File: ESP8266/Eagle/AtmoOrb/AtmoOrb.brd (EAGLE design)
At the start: 55.9 x 55.9 mm, 10 parts, among them J1 DCJ0202

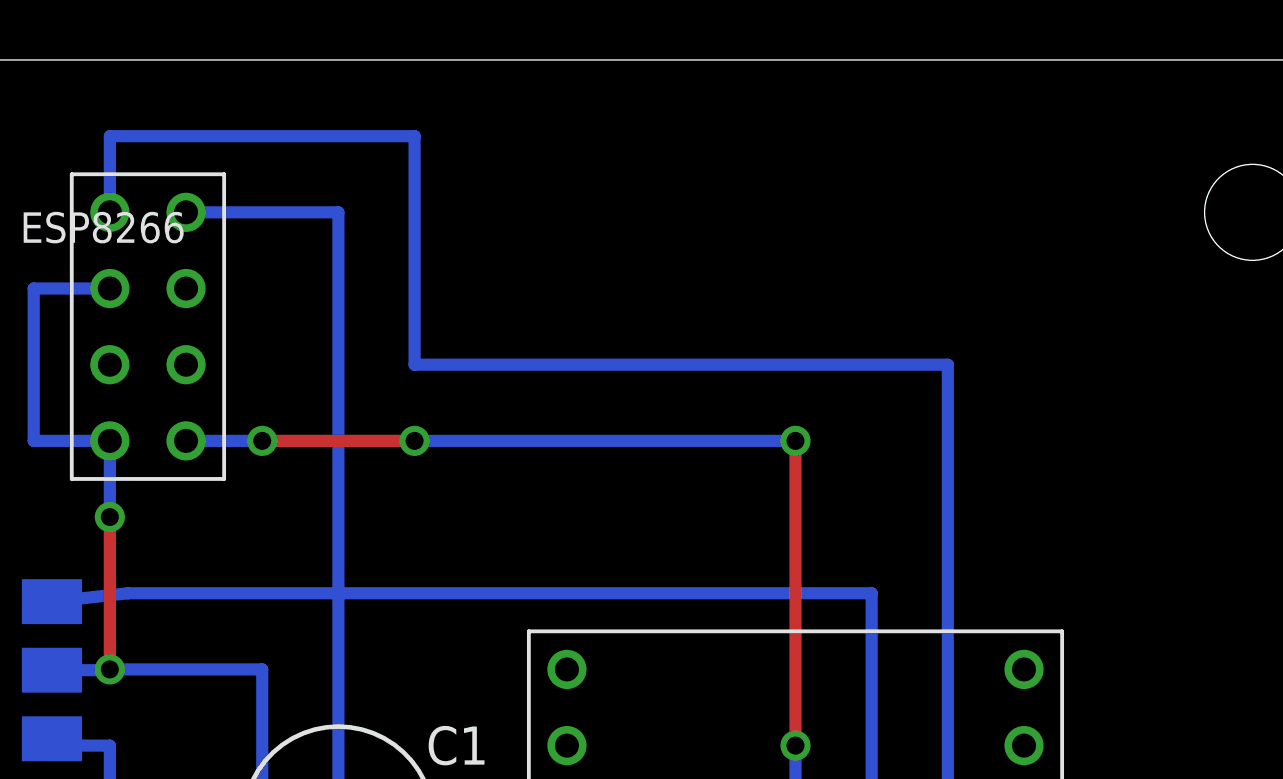
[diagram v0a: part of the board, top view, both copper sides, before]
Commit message: Added a switch to bring ESP8266 into update mode to schematic and board layout
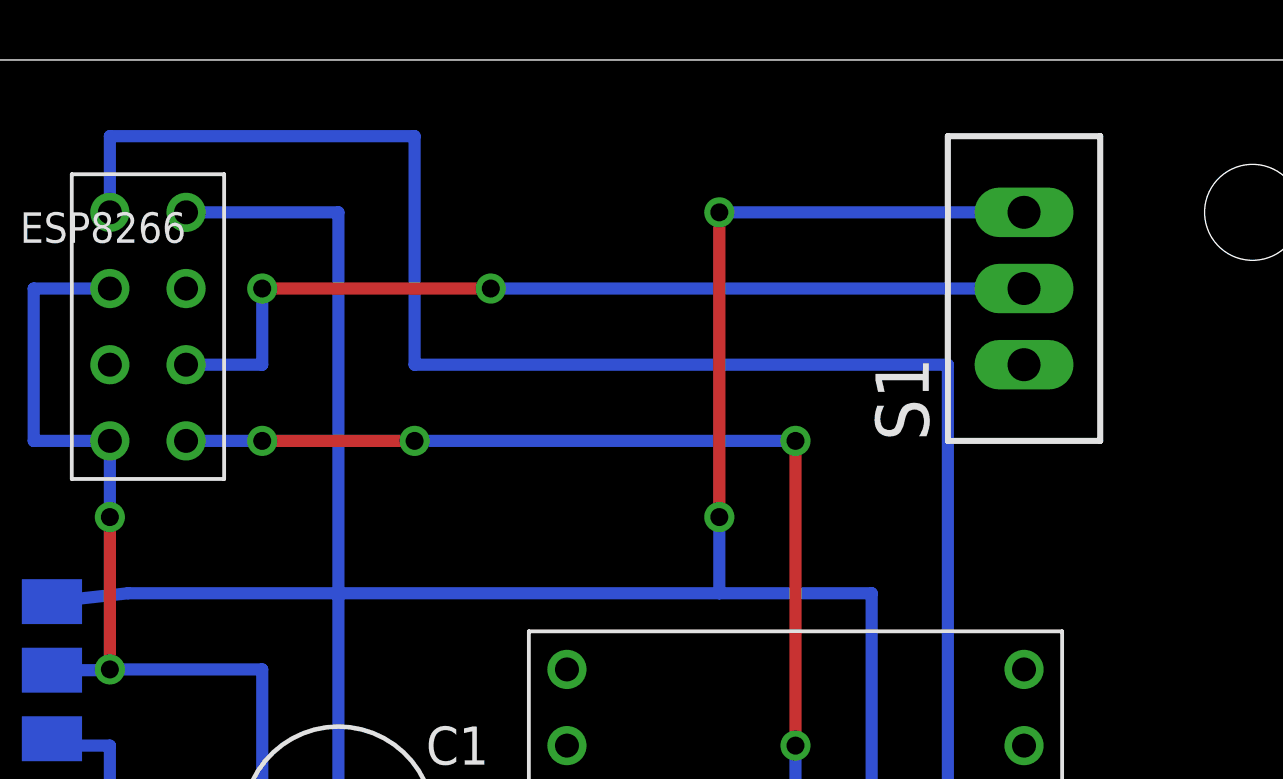
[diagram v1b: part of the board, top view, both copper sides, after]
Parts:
- added S1: TL32PO, switch:TL3XPO
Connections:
- new net N$6: ESP8266.7, S1.2
- net GND: now also S1.3
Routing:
- net N$6: track 0.00 -> 30.5 mm, vias 0 -> 2
- net GND: track 118.8 -> 141.6 mm, vias 0 -> 2
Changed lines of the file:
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@@
 <attribute name="OC_FARNELL" value="unknown" x="20.32" y="12.7" size="1.778" layer="27" rot="R270" display="off"/>
 </element>
+<element name="S1" library="switch" package="TL3XPO" value="TL32PO" x="43.18" y="48.26" rot="R90"/>
 </elements>
 <signals>
@@
 <wire x1="22.86" y1="30.48" x2="20.32" y2="30.48" width="0.4064" layer="16"/>
 <wire x1="20.32" y1="30.48" x2="20.32" y2="38.1" width="0.4064" layer="16"/>
-<wire x1="20.32" y1="38.1" x2="38.1" y2="38.1" width="0.4064" layer="16"/>
+<wire x1="20.32" y1="38.1" x2="33.02" y2="38.1" width="0.4064" layer="16"/>
+<wire x1="33.02" y1="38.1" x2="38.1" y2="38.1" width="0.4064" layer="16"/>
 <wire x1="15.24" y1="10.16" x2="15.24" y2="15.24" width="0.4064" layer="16"/>
 <wire x1="13.26" y1="20.32" x2="10.16" y2="20.32" width="0.4064" layer="16"/>
@@
 <wire x1="15.24" y1="15.24" x2="10.16" y2="15.24" width="0.4064" layer="16"/>
 <wire x1="10.16" y1="15.24" x2="10.16" y2="15.52" width="0.4064" layer="16"/>
+<contactref element="S1" pad="3"/>
+<wire x1="43.18" y1="50.8" x2="33.02" y2="50.8" width="0.4064" layer="16"/>
+<via x="33.02" y="50.8" extent="1-16" drill="0.6" shape="square"/>
+<wire x1="33.02" y1="50.8" x2="33.02" y2="40.64" width="0.4064" layer="1"/>
+<via x="33.02" y="40.64" extent="1-16" drill="0.6" shape="square"/>
+<wire x1="33.02" y1="40.64" x2="33.02" y2="38.1" width="0.4064" layer="16"/>
 </signal>
 <signal name="+5V">
@@
 <wire x1="33.02" y1="27.94" x2="27.94" y2="27.94" width="0.4064" layer="16"/>
 </signal>
+<signal name="N$6">
+<contactref element="ESP8266" pad="7"/>
+<contactref element="S1" pad="2"/>
+<wire x1="15.24" y1="45.72" x2="17.78" y2="45.72" width="0.4064" layer="16"/>
+<wire x1="17.78" y1="45.72" x2="17.78" y2="48.26" width="0.4064" layer="16"/>
+<via x="17.78" y="48.26" extent="1-16" drill="0.6" shape="square"/>
+<wire x1="17.78" y1="48.26" x2="25.4" y2="48.26" width="0.4064" layer="1"/>
+<via x="25.4" y="48.26" extent="1-16" drill="0.6" shape="square"/>
+<wire x1="25.4" y1="48.26" x2="43.18" y2="48.26" width="0.4064" layer="16"/>
+</signal>
 </signals>
